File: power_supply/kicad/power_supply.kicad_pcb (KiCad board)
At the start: 2 copper layers, 90 x 80 mm, 6 parts, among them J1 pcie_98, U2 ESD5344D

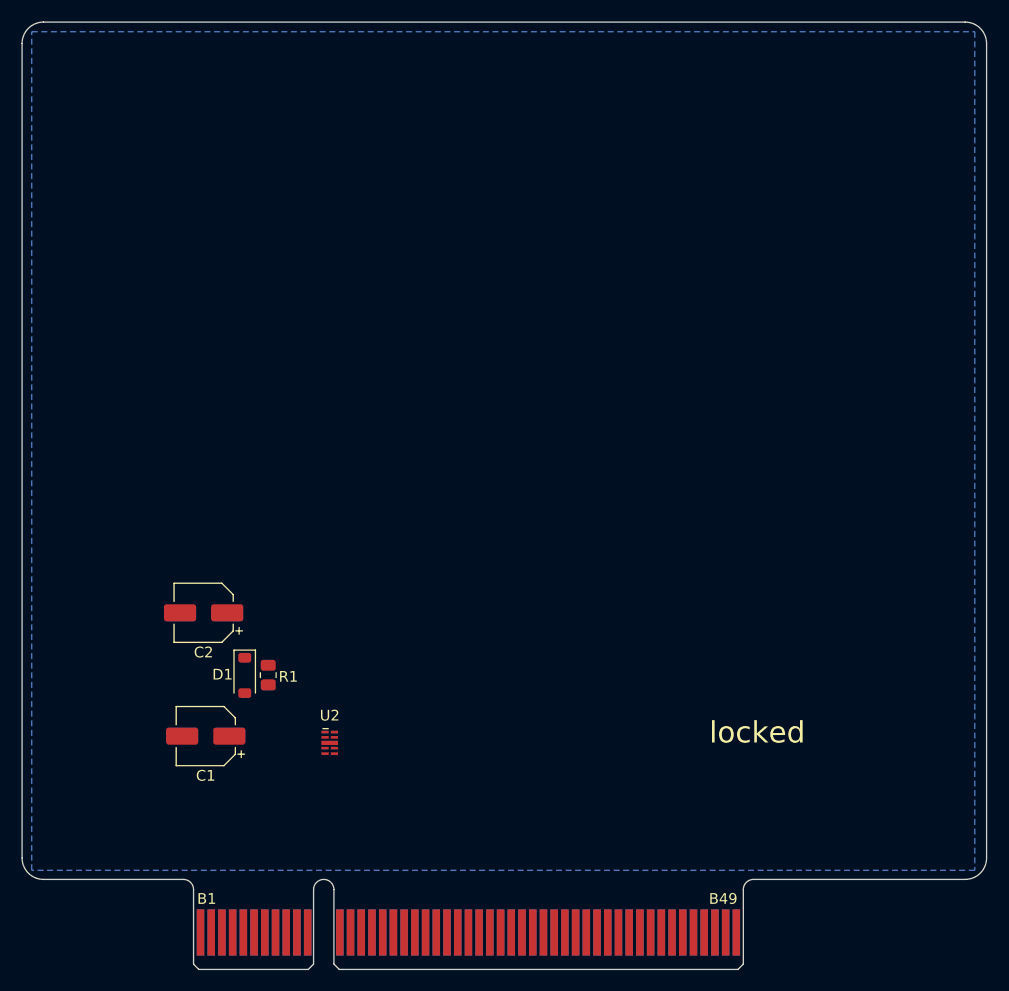
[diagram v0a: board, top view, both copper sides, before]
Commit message: Set up a skeleton design of the pwoer supply.
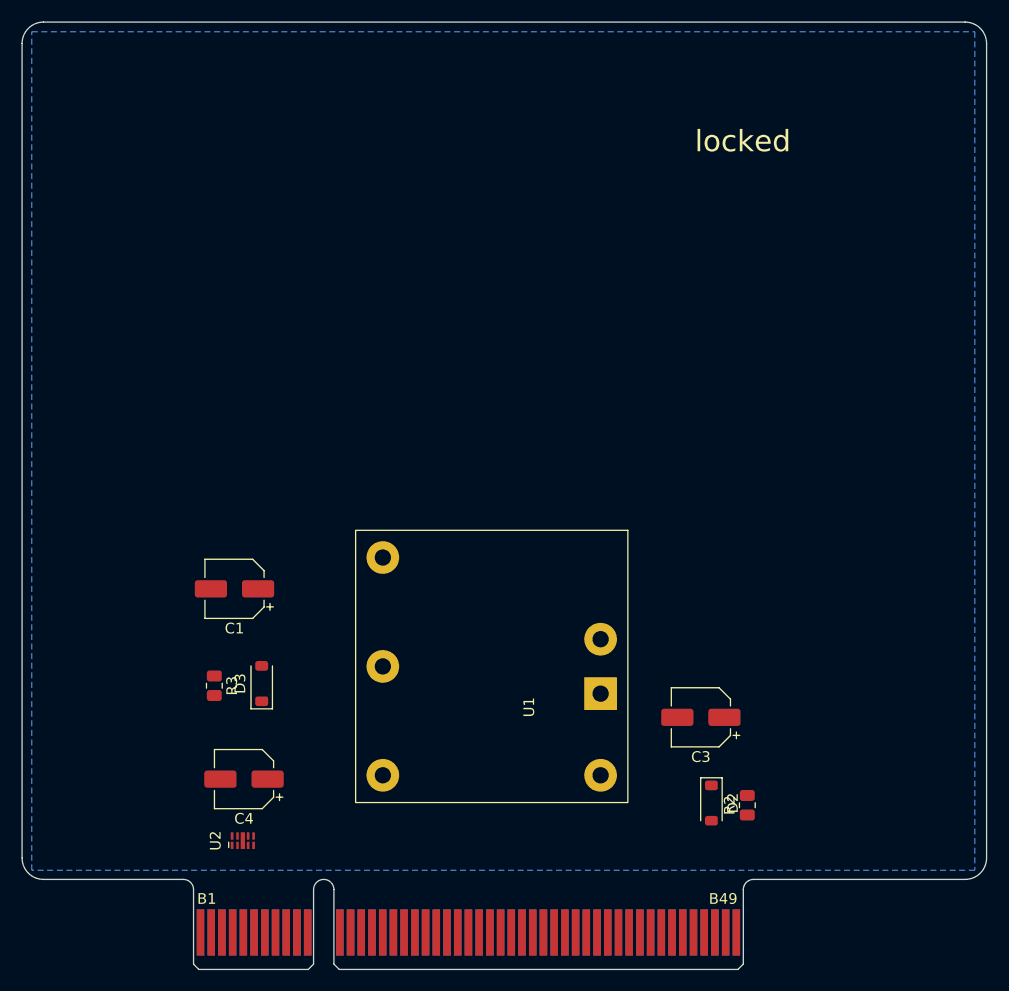
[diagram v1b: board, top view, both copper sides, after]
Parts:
- removed C2: 100uf, power_supply:CP_Elec_5x5.4_JLCPCB
- removed D1: B5819W SL, Diode_SMD:D_SOD-123
- removed R1: 0R, Resistor_SMD:R_0805_2012Metric
- added C3: 100uf 35V, power_supply:CP_Elec_5x5.4_JLCPCB, F.Cu at (105.2, 36.5)
- added C4: 100uf, power_supply:CP_Elec_5x5.4_JLCPCB, F.Cu at (62.6, 42.2)
- added D2: B5819W SL, Diode_SMD:D_SOD-123, F.Cu at (106.2, 44.5)
- added D3: B5819W SL, Diode_SMD:D_SOD-123, F.Cu at (64.2, 33.3)
- added R2: 0R, Resistor_SMD:R_0805_2012Metric, F.Cu at (109.5, 44.7)
- added R3: 0R, Resistor_SMD:R_0805_2012Metric, F.Cu at (59.8, 33.5)
- added U1: URB2405YMD-10WR3, power_supply:DCDC, F.Cu at (85.7, 31.7)
- moved C1 14.0 mm to (61.7, 24.5)
- moved U2 12.2 mm to (62.5, 48.0), turned to 90 degrees
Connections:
- C1 pad 1: /+5VBUS -> Net-(D3-A)
- J1 pad A48: unconnected-(J1-Pin_a48-PadA48) -> /VIN-
- J1 pad A49: unconnected-(J1-Pin_a49-PadA49) -> /VIN-
- J1 pad B1: /+5v -> /+5V
- J1 pad B2: /+5v -> /+5V
- J1 pad B3: /+5v -> /+5V
- J1 pad B4: /+5v -> /+5V
- J1 pad B48: unconnected-(J1-Pin_b48-PadB48) -> /VIN+
- J1 pad B49: unconnected-(J1-Pin_b49-PadB49) -> /VIN+
- U2 pad 1: unconnected-(U2-D1-Pad1) -> /+5V
- U2 pad 2: unconnected-(U2-D2-Pad2) -> /+5V
- U2 pad 4: unconnected-(U2-D3-Pad4) -> /+5V
- U2 pad 5: unconnected-(U2-D4-Pad5) -> /+5V

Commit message: Added LEDs, test points, and LCSC ids.
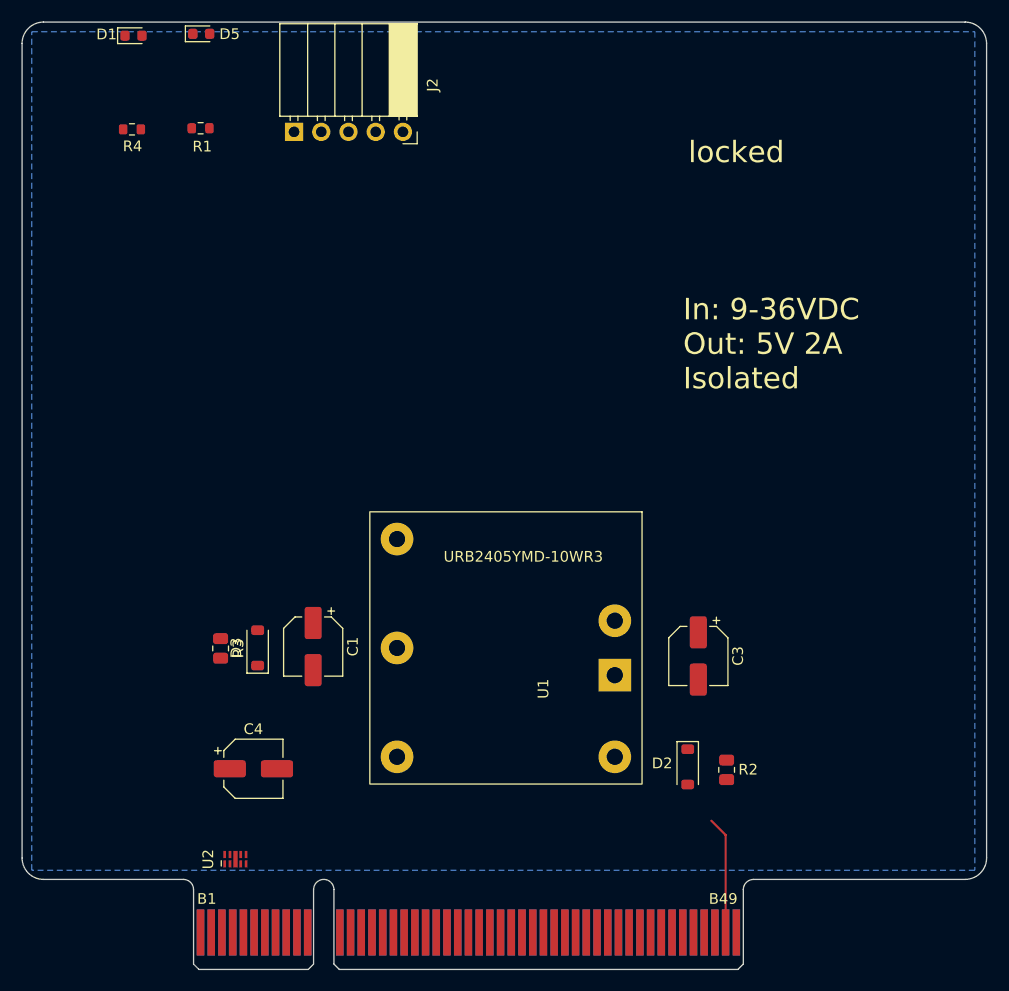
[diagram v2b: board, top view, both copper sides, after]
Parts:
- added D1: LED, LED_SMD:LED_0603_1608Metric, F.Cu at (52.2, -27.1)
- added D5: LED, LED_SMD:LED_0603_1608Metric, F.Cu at (58.6, -27.3)
- added J2: Conn_01x05_Socket, power_supply:PinSocket_1x05_P2.54mm_Horizontal, F.Cu at (77.4, -18.2)
- added R1: 3K9, Resistor_SMD:R_0603_1608Metric, F.Cu at (58.5, -18.5)
- added R4: 20K, Resistor_SMD:R_0603_1608Metric, F.Cu at (52.1, -18.4)
- moved C1 9.10 mm to (69.0, 29.9), turned to 90 degrees
- moved C3 5.73 mm to (105.0, 30.7), turned to 90 degrees
- moved D2 4.04 mm to (104.0, 41.1)
- moved R2 3.82 mm to (107.6, 41.4)
- moved R3 3.53 mm to (60.4, 30.0)
- moved D3 3.35 mm to (63.8, 30.0)
- moved U1 2.18 mm to (87.0, 30.0)
- moved U2 1.86 mm to (61.8, 49.7)
- moved C4 1.30 mm to (63.4, 41.3), turned to 180 degrees
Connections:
- U2 pad 4: /+5V -> unconnected-(U2-D3-Pad4)
- U2 pad 5: /+5V -> unconnected-(U2-D4-Pad5)
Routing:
- net /VIN+: track 0.00 -> 11.0 mm
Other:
- board text added: "In: 9-36VDC Out: 5V 2A Isolated"
- board text added: "URB2405YMD-10WR3"

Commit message: More cleanup of the power supply's PCB. Not done.
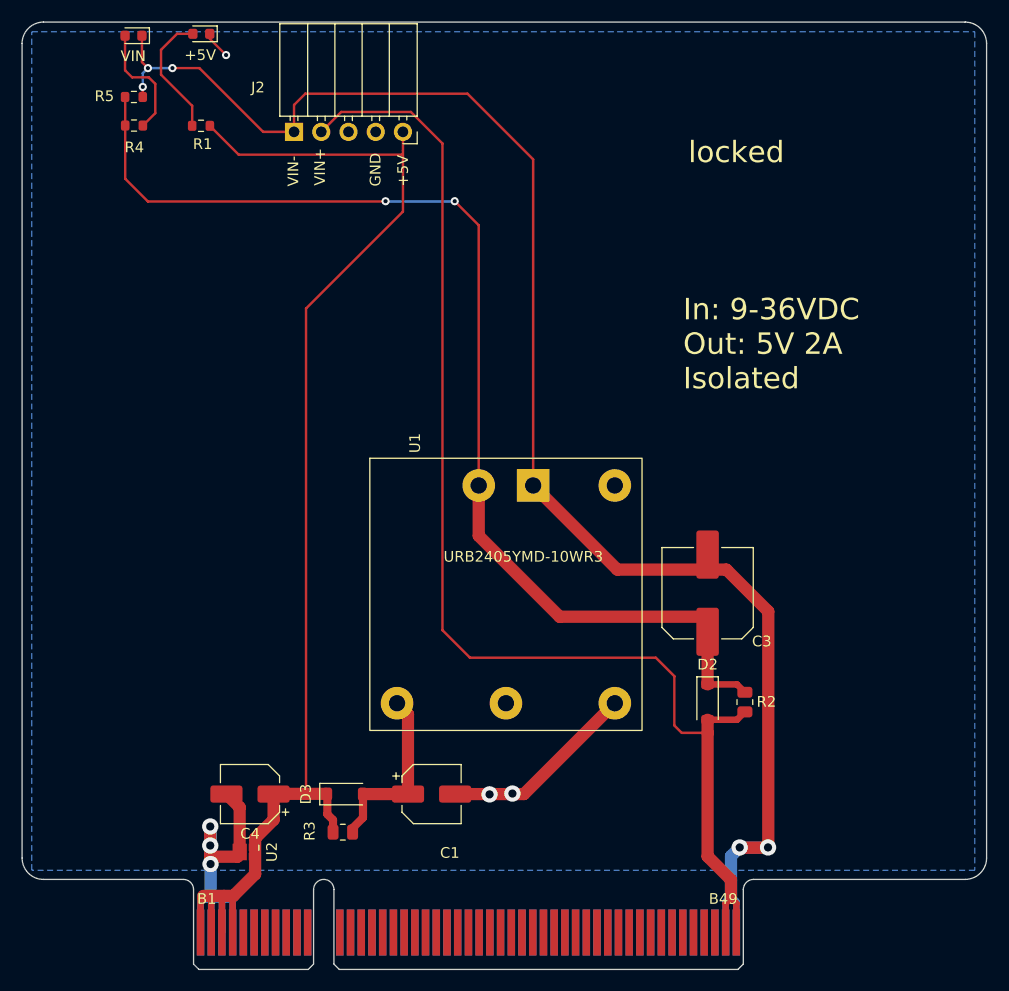
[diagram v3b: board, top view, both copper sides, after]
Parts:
- added R5: 100K, Resistor_SMD:R_0603_1608Metric, F.Cu at (52.3, -21.4)
- C1, C4: value 100uf -> 100uf 10V
- C3: value 100uf 35V -> 100uf 50V; footprint power_supply:CP_Elec_5x5.4_JLCPCB -> power_supply:C_Elec_8x10.2_JLCPCB
- D1: value LED -> LED YELLOW
- D5: value LED -> LED GREEN
- moved R3 20.6 mm to (71.8, 47.2), turned to 180 degrees
- moved C1 17.7 mm to (80.1, 43.6), turned to 180 degrees
- moved D3 15.9 mm to (72.0, 43.6), turned to 0 degrees
- moved R2 6.55 mm to (109.3, 35.1)
- moved D2 6.32 mm to (105.8, 35.1)
- moved C3 5.92 mm to (105.8, 24.9), turned to -90 degrees
- moved U1 5.00 mm to (87.0, 25.0), turned to 0 degrees
- moved C4 2.38 mm to (63.1, 43.6), turned to 0 degrees
- moved U2 1.10 mm to (62.6, 49.0), turned to -90 degrees
- moved R4 0.40 mm to (52.3, -18.7)
- moved R1 0.23 mm to (58.5, -18.7)
- turned D1 to 180 degrees
- turned D5 to 180 degrees
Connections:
- U2 pad 4: unconnected-(U2-D3-Pad4) -> GND
- U2 pad 5: unconnected-(U2-D4-Pad5) -> GND
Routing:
- net /VIN-: track 0.00 -> 146.7 mm, vias 0 -> 5
- net /+5V: track 0.00 -> 121.1 mm
- net /VIN+: track 11.0 -> 118.3 mm
- net Net-(D2-K): track 0.00 -> 106.0 mm, vias 0 -> 2
- net GND: track 0.00 -> 58.1 mm, vias 0 -> 6
- net Net-(D3-A): track 0.00 -> 16.8 mm
- net Net-(D5-A): track 0.00 -> 11.9 mm
- net Net-(D1-A): track 0.00 -> 10.9 mm
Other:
- board text added: "+5V"
- board text added: "GND"
- board text added: "VIN"
- board text added: "VIN+"
- board text added: "VIN-"

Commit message: Completed the power supply PCB cleanup TODO list. Needs final review.
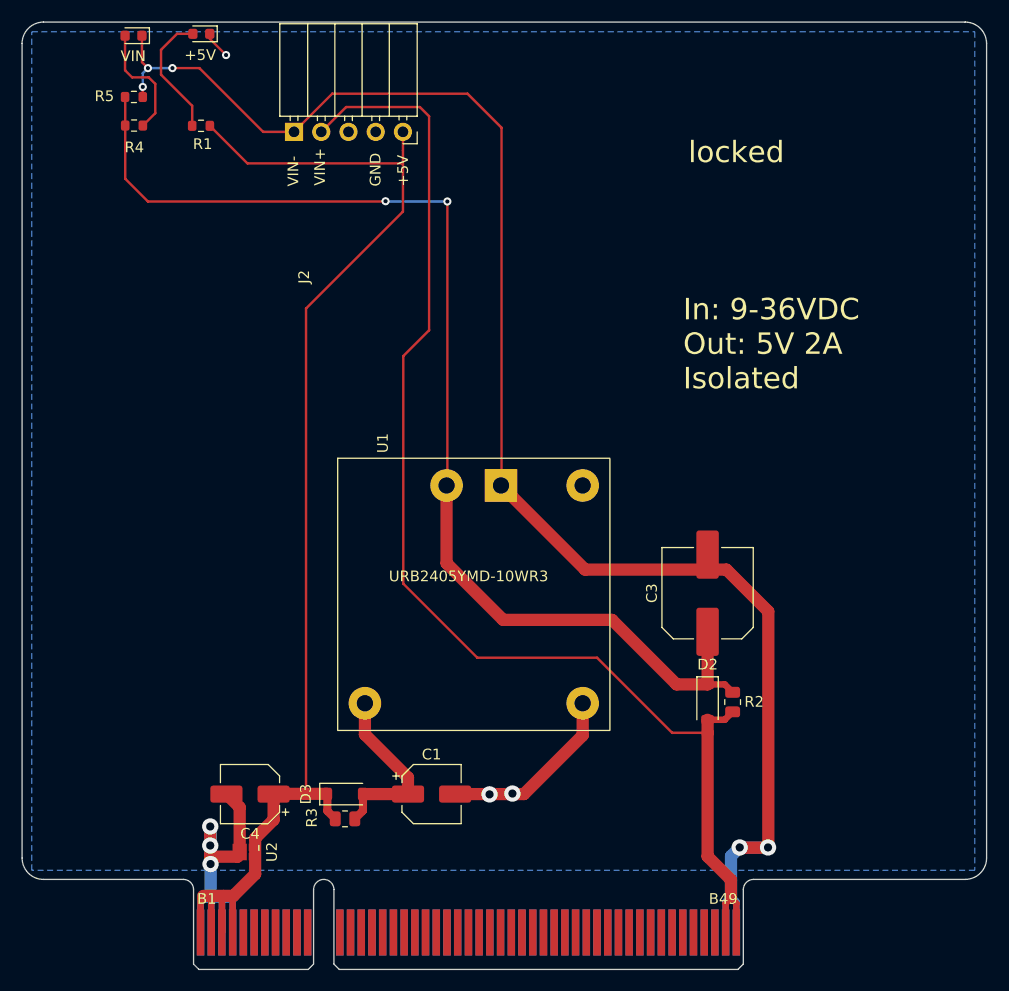
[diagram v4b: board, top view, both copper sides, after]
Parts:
- C1, C4: footprint power_supply:CP_Elec_5x5.4_JLCPCB -> Capacitor_SMD:CP_Elec_5x5.4
- C3: footprint power_supply:C_Elec_8x10.2_JLCPCB -> Capacitor_SMD:C_Elec_8x10.2
- moved J2 5.08 mm to (72.3, -18.2), turned to 0 degrees
- moved U1 3.00 mm to (84.0, 25.0)
- moved R3 1.26 mm to (72.0, 45.9)
- moved R2 1.14 mm to (108.2, 35.1)
- turned C1 to 0 degrees
- turned C3 to 90 degrees
- turned C4 to 180 degrees
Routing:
- net Net-(D2-K): track 106.0 -> 109.0 mm
- net GND: track 58.1 -> 56.9 mm
- net /VIN+: track 118.3 -> 117.2 mm
- net /+5V: track 121.1 -> 120.3 mm
